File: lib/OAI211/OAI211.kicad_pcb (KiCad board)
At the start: 2 copper layers, 8 parts

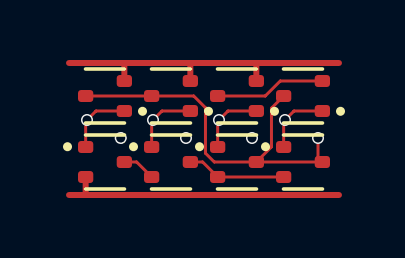
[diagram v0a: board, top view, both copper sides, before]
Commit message: All cells now use 1mm*4mm grid rather than 1.1mm*4.4mm
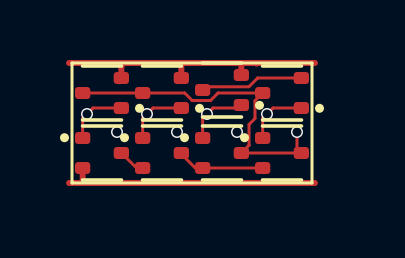
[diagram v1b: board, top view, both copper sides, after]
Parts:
- moved N4 0.76 mm to (7.00, 3.00)
- moved P4 0.71 mm to (7.00, 1.00)
- moved N3 0.58 mm to (5.00, 3.00)
- moved P3 0.54 mm to (5.00, 0.90)
- moved N2 0.42 mm to (3.00, 3.00)
- moved N1 0.32 mm to (1.00, 3.00)
- moved P2 0.32 mm to (3.00, 1.00)
- moved P1 0.14 mm to (1.00, 1.00)
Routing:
- net Y: track 13.1 -> 11.3 mm
- net VDD: track 10.8 -> 9.79 mm
- net GND: track 9.61 -> 8.70 mm

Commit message: Make the pads of my SOT523 footprint very slightly smaller, which is enough to route all the cells and leave the mosfets exactly on the grid
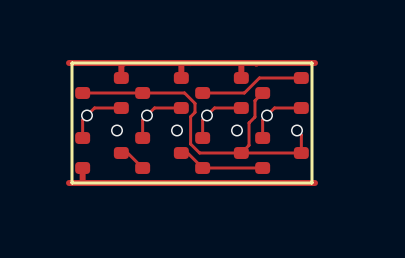
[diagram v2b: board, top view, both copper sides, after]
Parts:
- N1, N2, N3, N4, P1, P2, P3, P4: footprint Package_TO_SOT_SMD:SOT-523 -> RV523:SOT523
- moved P3 0.10 mm to (5.00, 1.00)
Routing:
- net Y: track 11.3 -> 12.2 mm

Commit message: Propagate MOSFET values to the cells' PCBs
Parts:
- N1, N2, N3, N4: value (none) -> NMOS
- P1, P2, P3, P4: value (none) -> PMOS
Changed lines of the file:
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@@
 			)
 		)
-		(property "Value" ""
+		(property "Value" "PMOS"
 			(at 0 0 180)
 			(layer "F.Fab")
@@
 			)
 		)
-		(property "Value" ""
+		(property "Value" "PMOS"
 			(at 0 0 180)
 			(layer "F.Fab")
@@
 			)
 		)
-		(property "Value" ""
+		(property "Value" "NMOS"
 			(at 0 0 0)
 			(layer "F.Fab")
@@
 			)
 		)
-		(property "Value" ""
+		(property "Value" "NMOS"
 			(at 0 0 0)
 			(layer "F.Fab")
@@
 			)
 		)
-		(property "Value" ""
+		(property "Value" "NMOS"
 			(at 0 0 0)
 			(layer "F.Fab")
@@
 			)
 		)
-		(property "Value" ""
+		(property "Value" "PMOS"
 			(at 0 0 180)
 			(layer "F.Fab")
@@
 			)
 		)
-		(property "Value" ""
+		(property "Value" "NMOS"
 			(at 0 0 0)
 			(layer "F.Fab")
@@
 			)
 		)
-		(property "Value" ""
+		(property "Value" "PMOS"
 			(at 0 0 180)
 			(layer "F.Fab")
